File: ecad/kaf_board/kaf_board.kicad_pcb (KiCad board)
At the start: 4 copper layers, 116 x 71 mm, 233 parts, among them J1 PWR, J2 TEC1, J3 Conn_01x12, J4 TEC2, J5 USB, J6 TECPWR, M1 Motor_Servo, M2 Servo cut-out, Q1 MMBT3904LT1G, Q2 NTD4804N, Q3 NTD4804N, U1 MAX4649, U10 LM224, U11 LM224, U12 LM224, U13 LD1117S12CTR_SOT223, U14 LD1117S33CTR_SOT223, U15 MAX743, U16 93LCxxBxxOT, U17 FT2232HL, U18 ICE40HX1K-VQ100, U19 W25X20CL, U2 ADP7118AUJZ, U20 MCP3004, U21 TC4427, U3 AD9826, U4 KAF-CDIP24, U5 TL432LIAIDBZR, U6 TL432LIAIDBZR, U7 TC4427, U8 TC4427, U9 TC4428, X1 KC7050A-C3, Y1 12 MHz

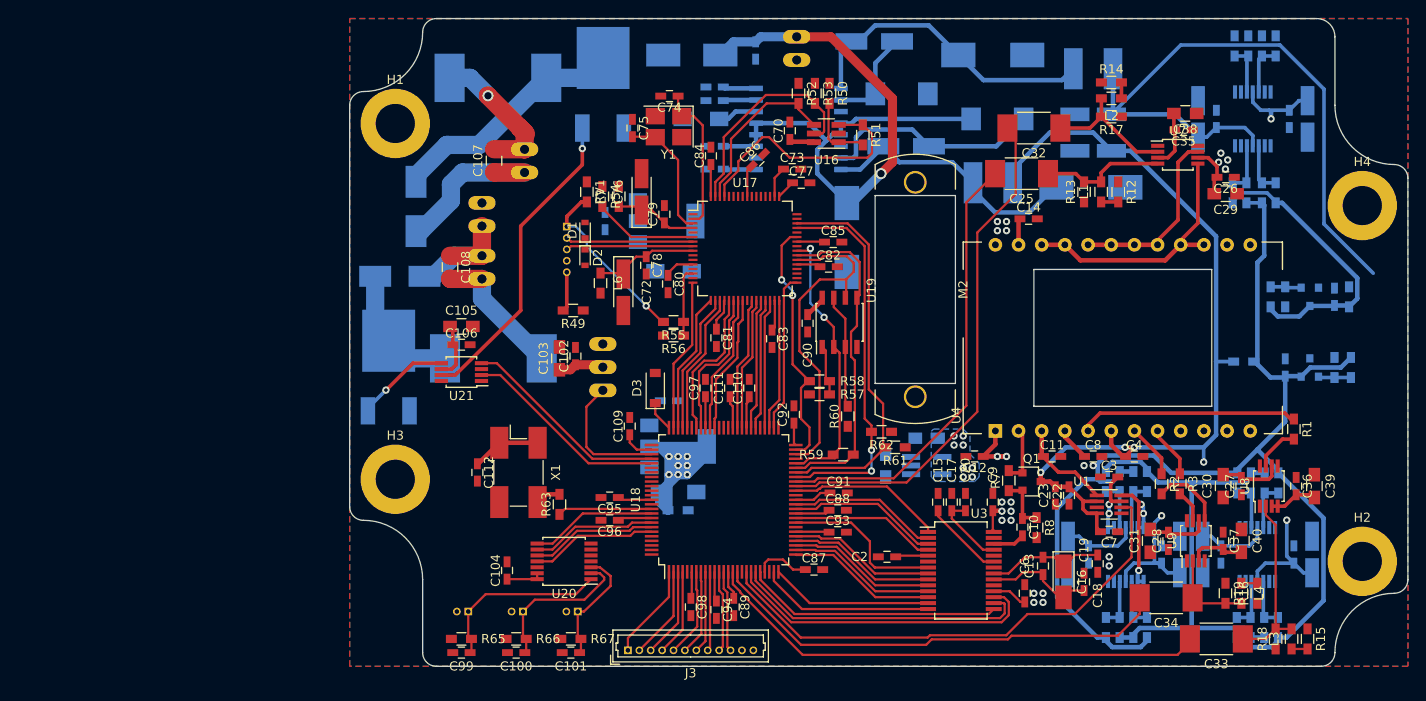
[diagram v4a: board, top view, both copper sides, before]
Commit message: Most things connected on PCB except GND. Doing ERC.
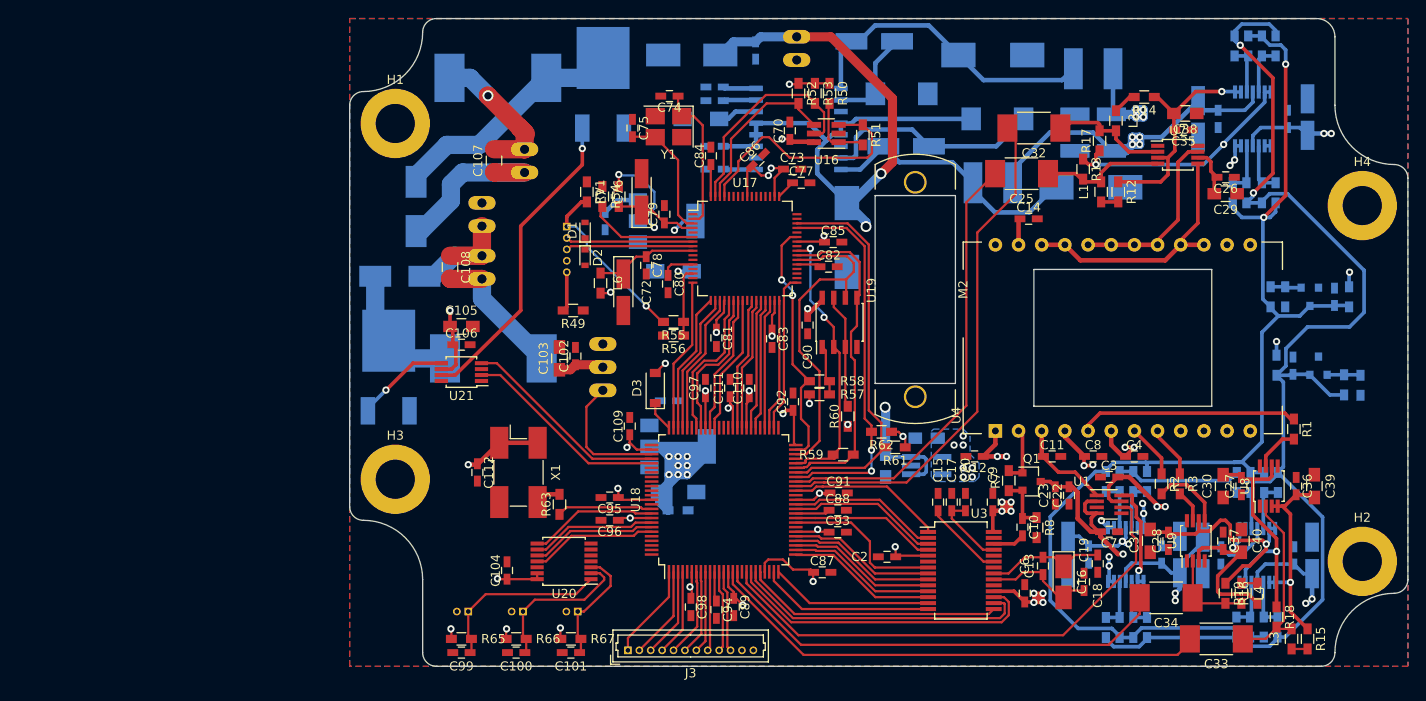
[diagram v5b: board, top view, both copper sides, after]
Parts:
- moved R36 16.5 mm to (189.2, 117.8), turned to 270 degrees
- moved R38 16.5 mm to (193.8, 117.8), turned to 270 degrees
- moved R42 16.5 mm to (189.2, 133.7), turned to 90 degrees
- moved R40 16.4 mm to (193.7, 133.7), turned to 90 degrees
- moved R37 16.0 mm to (190.8, 117.8), turned to 90 degrees
- moved R39 16.0 mm to (192.2, 117.8), turned to 90 degrees
- moved R43 15.9 mm to (190.7, 133.7), turned to 270 degrees
- moved R41 15.9 mm to (192.2, 133.7), turned to 270 degrees
- moved C48 12.0 mm to (197.0, 77.8)
- moved C51 12.0 mm to (185.5, 125.8), turned to 270 degrees
- moved C52 12.0 mm to (197.5, 125.8), turned to 270 degrees
- moved C47 12.0 mm to (185.0, 78.0)
- moved C49 8.00 mm to (187.5, 125.8), turned to 90 degrees
- moved C50 8.00 mm to (195.5, 125.8), turned to 270 degrees
- moved C45 7.80 mm to (187.2, 78.0)
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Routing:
- net +15V: track 162.4 -> 87.8 mm, vias 5 -> 8
- net +3V3: track 74.6 -> 127.6 mm, vias 0 -> 33
- net /ccd/-V_REF: track 84.5 -> 132.6 mm, vias 0 -> 2
- net +6V: track 82.3 -> 123.6 mm, vias 1 -> 3
- net -15V: track 94.7 -> 59.2 mm, vias 0 -> 13
- net /ccd/V_VH: track 5.60 -> 32.0 mm, vias 0 -> 2
- net /ccd/V_RH: track 6.79 -> 28.2 mm, vias 0 -> 1
- net /ccd/V_VL: track 6.33 -> 25.2 mm, vias 0 -> 1
- net /ccd/V_HH: track 6.78 -> 25.6 mm, vias 0 -> 1
- net /ccd/V_RL: track 5.32 -> 22.2 mm, vias 0 -> 1
- net /ccd/+V_REF: track 127.8 -> 144.5 mm, vias 0 -> 2
- net /ccd/AVDD: track 7.48 -> 22.2 mm, vias 18 -> 15
- net /ccd/V_HL: track 6.12 -> 20.0 mm, vias 0 -> 1
- net /ccd/VGUARD: track 2.91 -> 6.91 mm, vias 8 -> 2
- net /ccd/VOG: track 6.40 -> 9.80 mm
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- added copper zone on In2.Cu, net +15V
- added copper zone on In2.Cu, net -15V

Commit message: PCB design finished. Will go over the traces once more.
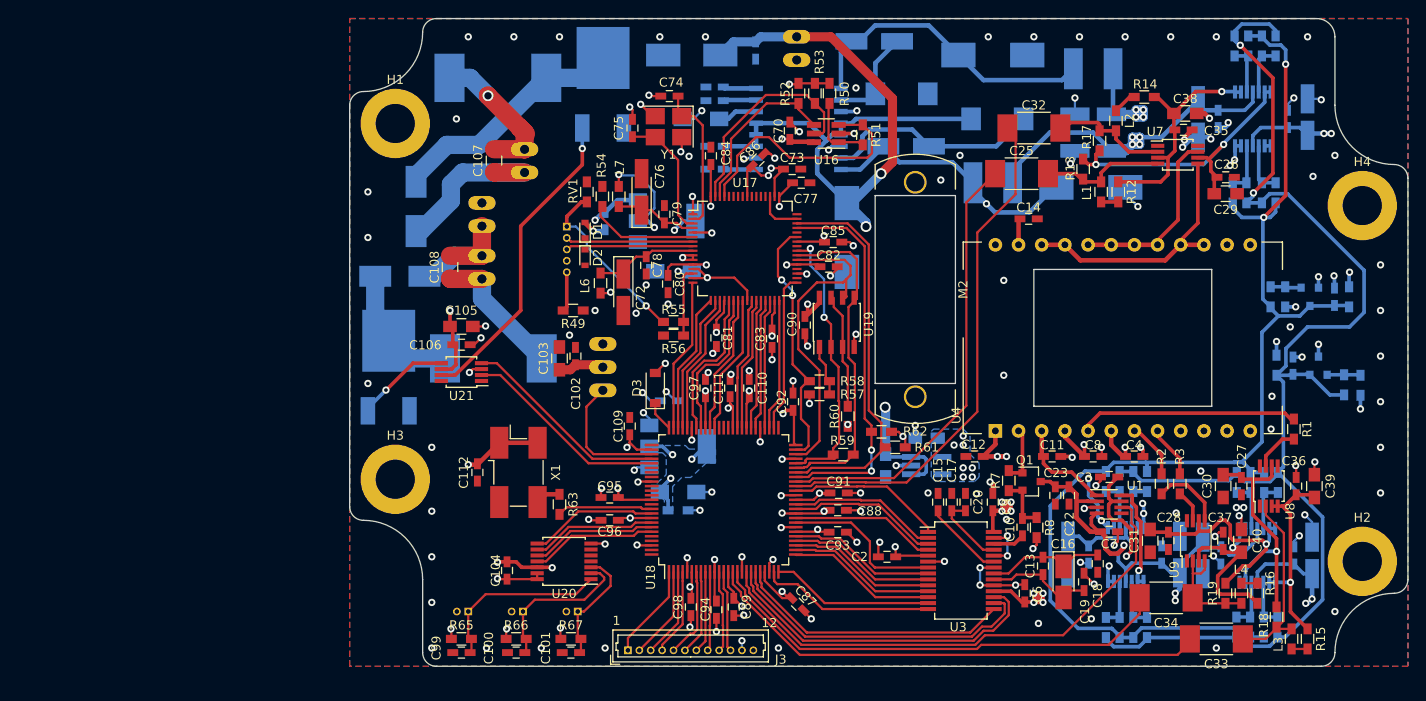
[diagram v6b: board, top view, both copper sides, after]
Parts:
- moved C87 4.42 mm to (141.1, 131.2), turned to 315 degrees
- moved C90 0.30 mm to (141.9, 100.6)
- moved U19 0.30 mm to (145.4, 100.3)
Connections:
- net +1V8 renamed /usb-interface/VREG
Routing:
- net GND: track 2.97 -> 176.7 mm, vias 0 -> 157
- net +1V2: track 54.7 -> 28.4 mm, vias 10 -> 8
- net +6V: track 123.6 -> 129.0 mm, vias 3 -> 6
- net /usb-interface/VREG: track 12.0 -> 16.8 mm, vias 0 -> 4
- net /ccd/VRD: track 7.50 -> 12.0 mm
- net +15V: track 87.8 -> 91.2 mm
- net Net-(C34-Pad1): track 9.66 -> 12.1 mm
- net /ccd/V_VH: track 32.0 -> 34.3 mm
- net -15V: track 59.2 -> 61.4 mm, vias 13 -> 10
- net /ccd/AD_SLOAD: track 34.8 -> 36.9 mm
- net /ccd/AD_SDATA: track 28.2 -> 30.3 mm
- net /ccd/AD_SCLK: track 32.5 -> 34.6 mm
- net +3V3: track 127.6 -> 125.9 mm
- net /ccd/VSS: track 9.59 -> 8.22 mm, vias 4 -> 3
- net /ccd/AMP_OFF: track 56.8 -> 58.1 mm
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- added copper zone on B.Cu, net +1V2
- added copper zone on In2.Cu, net /usb-interface/VREG
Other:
- board text added: "+"
- board text added: "-"
- board text added: "1"
- board text added: "12"
- board text added: "5.5 to 6V out"
- board text added: "5.5-6V"
- board text added: "DM"
- board text added: "DP"
- board text added: "GND"
- board text added: "PWM_servo"
- board text added: "SHIELD"
- board text added: "VTEC"
- board text added: "VUSB"

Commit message: Minor changes to PCB
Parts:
- added TP1: GND, Measurement_Points:Test_Point_Keystone_5005-5009_Compact, F.Cu at (202.8, 116.6)
- moved R18 0.20 mm to (193.4, 132.6)
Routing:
- net GND: track 176.7 -> 180.3 mm, vias 157 -> 158
- net +6V: track 129.0 -> 132.2 mm
- net /ccd/+V_REF: track 144.5 -> 146.5 mm
- net /ccd/-V_REF: track 133.3 -> 134.0 mm
- net +3V3: track 125.9 -> 126.5 mm
- net /ccd/AD_SDATA: track 30.3 -> 29.7 mm
- net Net-(C64-Pad1): vias 1 -> 0

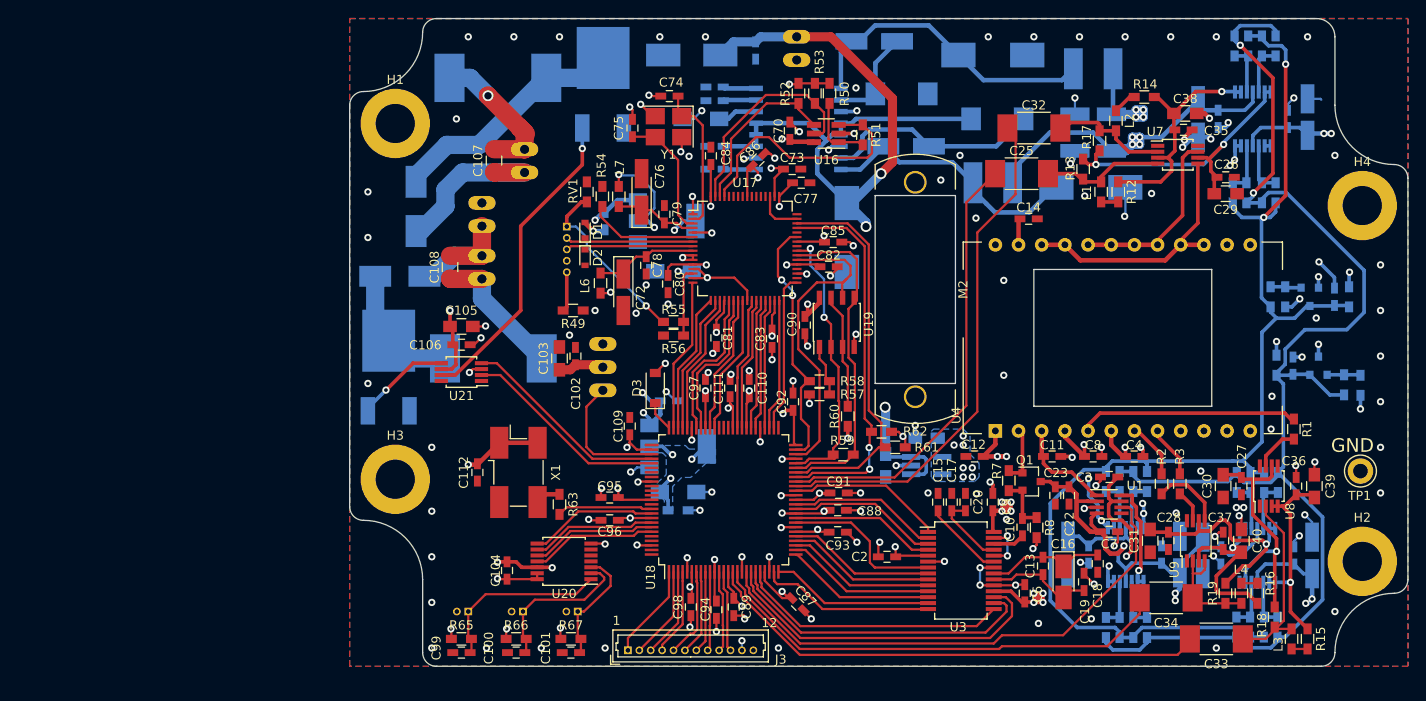
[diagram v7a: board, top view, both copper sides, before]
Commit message: Decided to ditch the TL432 in favour of a +-14.5V LDO regulator. Need to re-route a lot of stuff
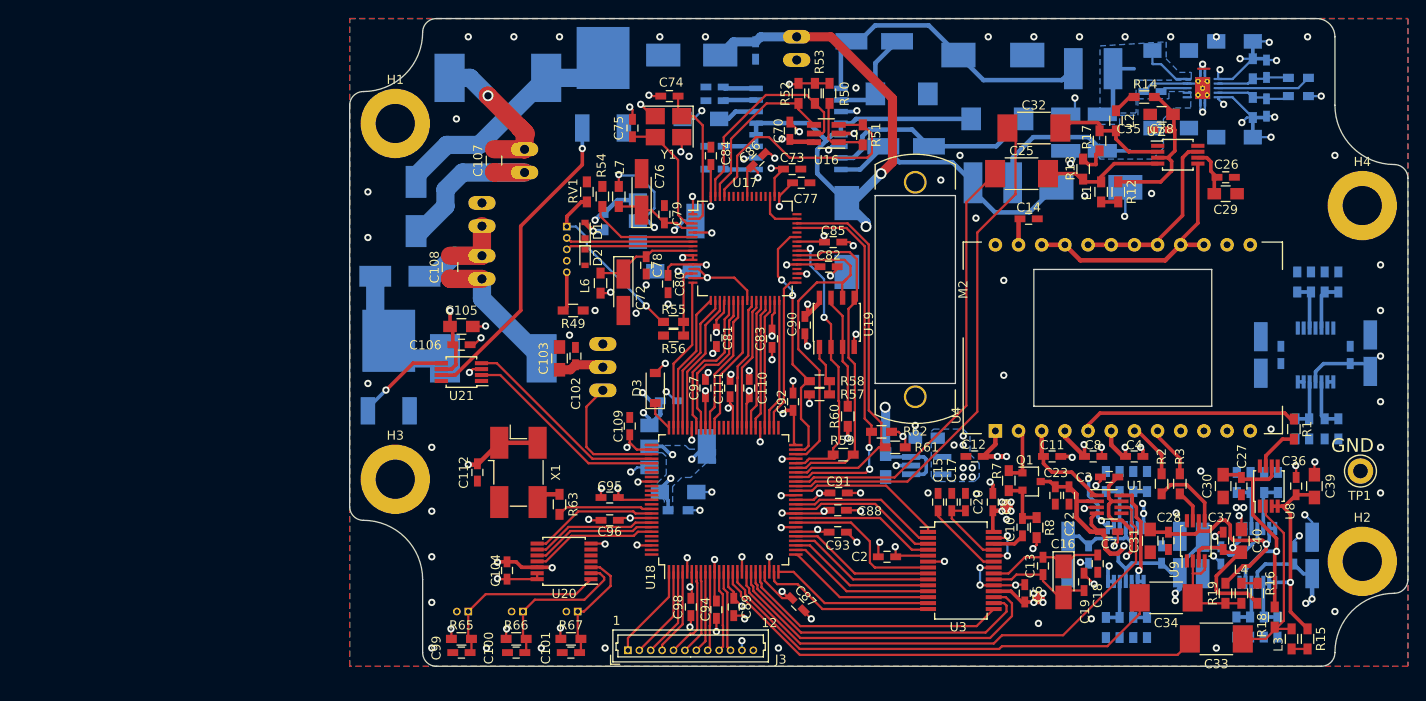
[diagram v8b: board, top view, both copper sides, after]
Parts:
- removed R10: 4.7k 0.1%, Resistors_SMD:R_0603_HandSoldering
- removed R11: 1k 0.1%, Resistors_SMD:R_0603_HandSoldering
- removed U6: TL432LIAIDBZR, TO_SOT_Packages_SMD:SOT-23
- added C113: 10n, Capacitors_SMD:C_0603_HandSoldering, B.Cu at (192.5, 72.5)
- added C114: 10u, Capacitors_SMD:C_1206_HandSoldering, B.Cu at (189.0, 80.0)
- added C115: 10u, Capacitors_SMD:C_1206_HandSoldering, B.Cu at (189.0, 69.5)
- added C67: 10u, Capacitors_SMD:C_1206_HandSoldering, B.Cu at (182.0, 70.5)
- added C71: 10n, Capacitors_SMD:C_0603_HandSoldering, B.Cu at (192.5, 76.8)
- C21: value 0.1u -> 10u; footprint Capacitors_SMD:C_0603_HandSoldering -> Capacitors_SMD:C_1206_HandSoldering
- R4: value 100 -> 169k 0.1%
- R5: value 4.7k 0.1% -> 12k 0.1%
- R6: value 1k 0.1% -> 147k 0.1%
- R63: value R22 -> 22
- R9: value 100 -> 15k 0.1%
- U5: value TL432LIAIDBZR -> TPS7A39; footprint TO_SOT_Packages_SMD:SOT-23 -> kaf_board:TI_WSON-10-1TP_3x3mm_P0.5mm_HandSolder
- moved C24 33.8 mm to (180.0, 75.0), turned to 0 degrees
- moved R9 29.6 mm to (196.0, 75.5), turned to 0 degrees
- moved C45 26.8 mm to (194.1, 103.9)
- moved C46 26.8 mm to (201.7, 103.9)
- moved C47 26.8 mm to (191.9, 103.9)
- moved C48 26.8 mm to (203.9, 103.7)
- moved R28 26.8 mm to (195.9, 95.9)
- moved R29 26.8 mm to (197.4, 95.9)
- moved R30 26.8 mm to (200.4, 95.9)
- moved R31 26.8 mm to (198.9, 95.9)
- moved R32 26.8 mm to (198.9, 112.0)
- moved R33 26.8 mm to (200.4, 112.0)
- moved R34 26.8 mm to (197.2, 112.0)
- moved R35 26.8 mm to (195.7, 112.0)
- moved U11 26.8 mm to (197.9, 103.9)
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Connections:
- C21 pad 1: /ccd/-V_REF -> GND
- C21 pad 2: GND -> /power/+15V
- C22 pad 2: +15V -> +14.5V
- C23 pad 2: +15V -> +14.5V
- C24 pad 2: /ccd/+V_REF -> Net-(C24-Pad2)
- C3 pad 2: -15V -> -14.5V
- C41 pad 2: +15V -> +14.5V
- C42 pad 2: -15V -> -14.5V
- C43 pad 1: +15V -> +14.5V
- C44 pad 2: -15V -> -14.5V
- C45 pad 2: +15V -> +14.5V
- C46 pad 2: -15V -> -14.5V
- C47 pad 1: +15V -> +14.5V
- C48 pad 2: -15V -> -14.5V
- C49 pad 2: +15V -> +14.5V
- C50 pad 2: -15V -> -14.5V
- C51 pad 1: +15V -> +14.5V
- C52 pad 2: -15V -> -14.5V
- C65 pad 1: +15V -> /power/+15V
- C66 pad 2: -15V -> /power/-15V
- C7 pad 2: +15V -> +14.5V
- L11 pad 2: +15V -> /power/+15V
- L12 pad 2: -15V -> /power/-15V
- Q1 pad 3: +15V -> +14.5V
- R20 pad 1: /ccd/+V_REF -> +14.5V
- R21 pad 2: /ccd/-V_REF -> -14.5V
- R22 pad 1: /ccd/+V_REF -> +14.5V
- R23 pad 2: /ccd/-V_REF -> -14.5V
- R24 pad 1: /ccd/+V_REF -> +14.5V
- R25 pad 2: /ccd/-V_REF -> -14.5V
- R26 pad 1: /ccd/+V_REF -> +14.5V
- R27 pad 2: /ccd/-V_REF -> -14.5V
- R28 pad 1: /ccd/+V_REF -> +14.5V
- R29 pad 2: /ccd/-V_REF -> -14.5V
- R30 pad 1: /ccd/+V_REF -> +14.5V
- R31 pad 2: /ccd/-V_REF -> -14.5V
- R32 pad 1: /ccd/+V_REF -> +14.5V
- R33 pad 2: /ccd/-V_REF -> -14.5V
- R34 pad 1: /ccd/+V_REF -> +14.5V
- R35 pad 2: /ccd/-V_REF -> -14.5V
- R36 pad 1: /ccd/+V_REF -> +14.5V
- R37 pad 2: /ccd/-V_REF -> -14.5V
- R38 pad 1: /ccd/+V_REF -> +14.5V
- R39 pad 2: /ccd/-V_REF -> -14.5V
- R4 pad 1: /ccd/-V_REF -> +14.5V
- R4 pad 2: -15V -> Net-(C71-Pad1)
- R40 pad 1: /ccd/+V_REF -> +14.5V
- R41 pad 2: /ccd/-V_REF -> -14.5V
- R42 pad 1: /ccd/+V_REF -> +14.5V
- R43 pad 2: /ccd/-V_REF -> -14.5V
- R5 pad 1: GND -> Net-(R5-Pad1)
- R5 pad 2: Net-(R5-Pad2) -> Net-(C113-Pad2)
- R6 pad 1: /ccd/-V_REF -> Net-(C113-Pad2)
- R6 pad 2: Net-(R5-Pad2) -> -14.5V
- R9 pad 1: /ccd/+V_REF -> Net-(C71-Pad1)
- R9 pad 2: +15V -> GND
- U1 pad 2: +15V -> +14.5V
- U1 pad 4: +15V -> +14.5V
- U1 pad 7: -15V -> -14.5V
- U10 pad 11: -15V -> -14.5V
- U10 pad 4: +15V -> +14.5V
- U11 pad 11: -15V -> -14.5V
- U11 pad 4: +15V -> +14.5V
- U12 pad 11: -15V -> -14.5V
- U12 pad 4: +15V -> +14.5V
- U5 pad 1: Net-(R5-Pad2) -> /power/+15V
- U5 pad 2: GND -> /power/+15V
- U5 pad 3: /ccd/-V_REF -> Net-(C24-Pad2)
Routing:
- net /ccd/+V_REF: track 146.5 -> 0.00 mm, vias 2 -> 0
- net /ccd/-V_REF: track 134.0 -> 0.00 mm, vias 2 -> 0
- net +15V: track 91.1 -> 0.00 mm, vias 8 -> 0
- net +14.5V: track 0.00 -> 64.3 mm, vias 0 -> 7
- net -15V: track 61.4 -> 0.00 mm, vias 10 -> 0
- net -14.5V: track 0.00 -> 54.9 mm, vias 0 -> 7
- net /ccd/V_VH: track 34.3 -> 8.83 mm, vias 2 -> 0
- net /power/+15V: track 0.00 -> 17.1 mm
- net /power/-15V: track 0.00 -> 13.1 mm
- net Net-(R5-Pad1): track 0.00 -> 10.4 mm
- net /ccd/V_VL: track 25.6 -> 17.2 mm, vias 1 -> 0
- net Net-(C71-Pad1): track 0.00 -> 8.10 mm
- net Net-(C113-Pad2): track 0.00 -> 8.00 mm
- net GND: track 180.3 -> 186.0 mm, vias 158 -> 147
- net Net-(R10-Pad2): track 3.67 -> 0.00 mm
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- added copper zone on In2.Cu, net +14.5V
- added copper zone on In2.Cu, net -14.5V
- added copper zone on B.Cu, net /power/+15V
- added copper zone on B.Cu, net /power/-15V
- removed copper zone on In2.Cu, net +15V
- removed copper zone on In2.Cu, net -15V
